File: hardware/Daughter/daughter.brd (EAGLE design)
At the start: 58.4 x 58.4 mm, 4 parts, among them J1 12V input

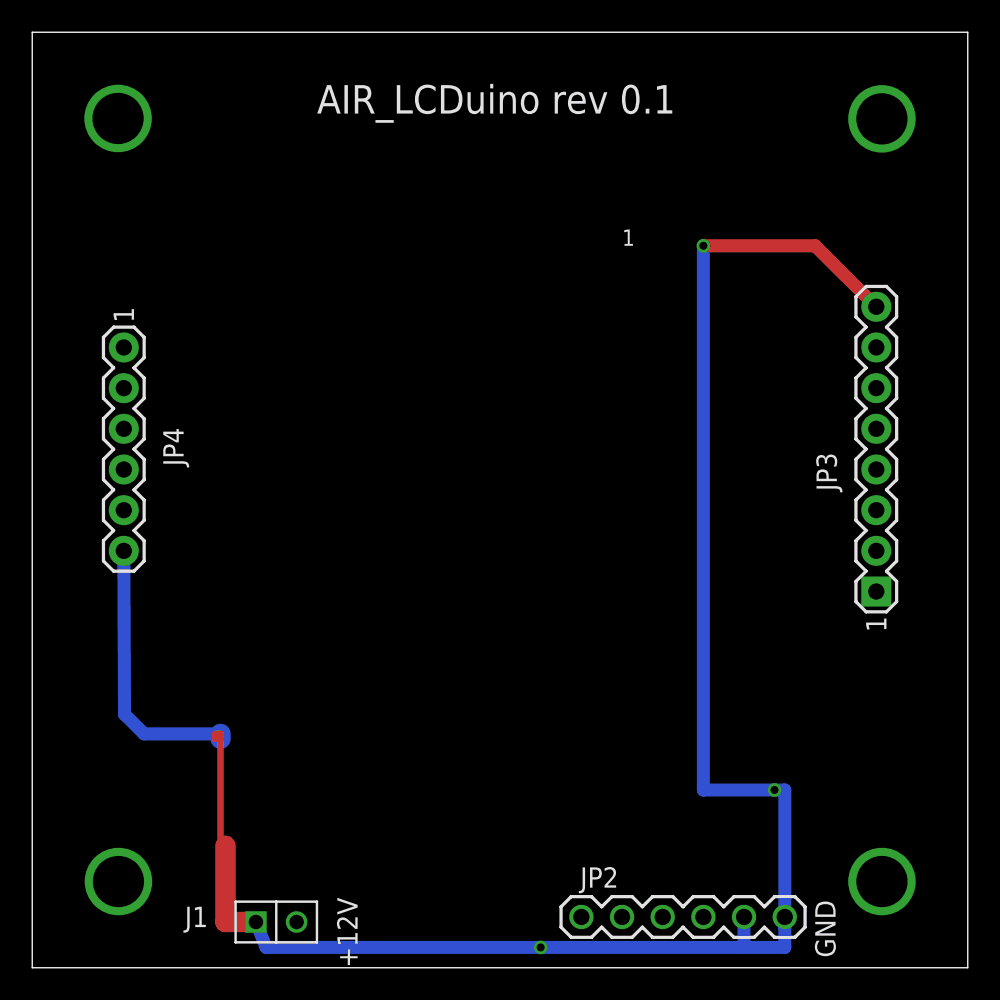
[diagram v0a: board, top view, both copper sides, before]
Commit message: added 12_adc_daughter/LTC2495_16x_pga_adc.pdf removed eagle.epf files and added gitignore file
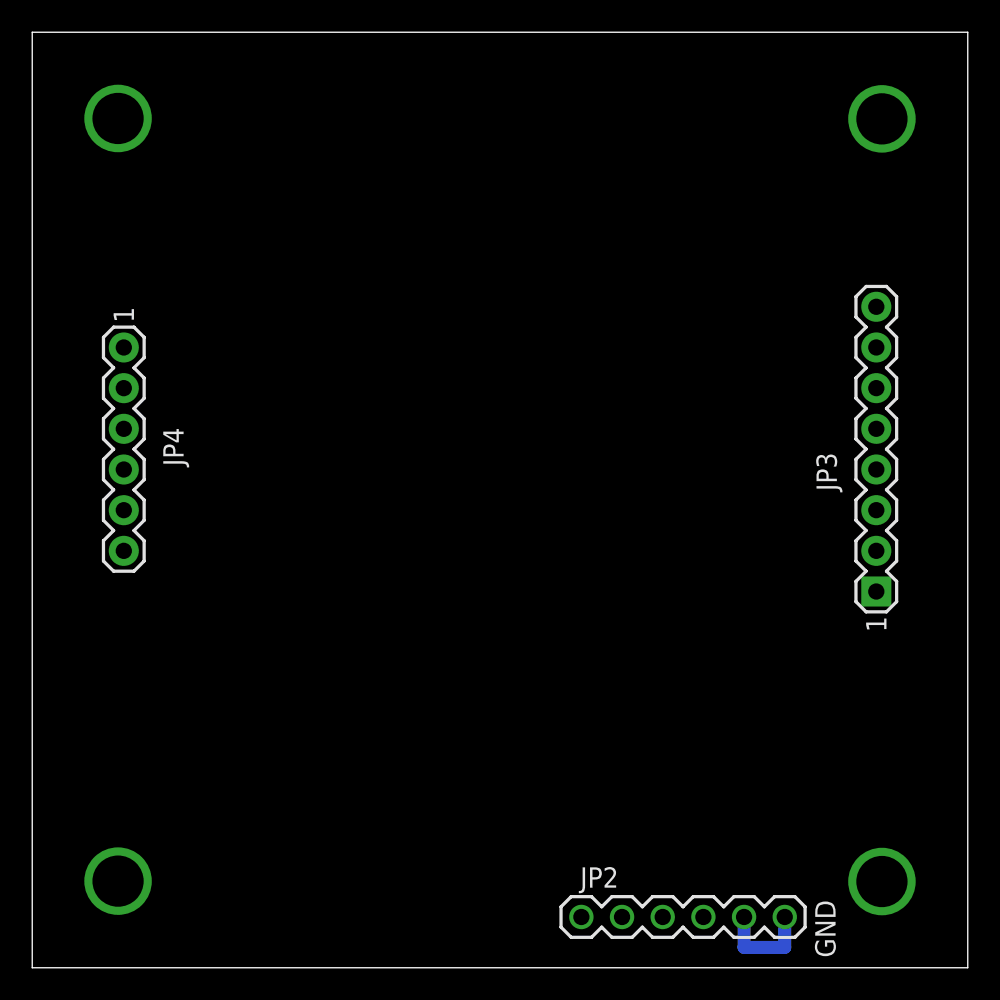
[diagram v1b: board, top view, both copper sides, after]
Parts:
- removed J1: 12V input, dp_devices:M1X2
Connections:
- removed net +12V: J1.2
- removed net +3.3V: JP4.5
- removed net +5V: JP3.1, JP4.1
- removed net RESET: JP3.2
- net GND: no longer J1.1, JP3.8, JP4.6
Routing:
- net GND: track 130.5 -> 6.34 mm, vias 3 -> 0
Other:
- board text removed: "+12V"
- board text removed: "1"
- board text removed: "AIR_LCDuino rev 0.1"
- board text removed: "RV-Builders Products"
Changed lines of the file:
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@@
 <board>
 <plain>
-<circle x="31.75" y="31.75" radius="28.448" width="0.0254" layer="199"/>
 <circle x="7.9248" y="55.5752" radius="1.524" width="0.0254" layer="199"/>
 <circle x="55.5752" y="55.5752" radius="1.524" width="0.0254" layer="199"/>
 <circle x="7.9248" y="7.9248" radius="1.524" width="0.0254" layer="199"/>
 <circle x="55.5752" y="7.9248" radius="1.524" width="0.0254" layer="199"/>
-<circle x="31.8516" y="16.51" radius="4.4958" width="0.0254" layer="199"/>
-<circle x="31.8516" y="16.51" radius="7.493" width="0.0254" layer="199"/>
-<circle x="15.875" y="16.8402" radius="2.5146" width="0.0254" layer="199"/>
-<circle x="13.7414" y="51.6128" radius="0.9906" width="0.0254" layer="199"/>
-<circle x="49.7586" y="51.6128" radius="0.9906" width="0.0254" layer="199"/>
-<circle x="13.7414" y="21.1074" radius="0.9144" width="0.0254" layer="199"/>
-<circle x="49.7586" y="21.1074" radius="0.9144" width="0.0254" layer="199"/>
-<wire x1="11.7602" y1="21.1074" x2="15.748" y2="21.1074" width="0.0254" layer="199" curve="180"/>
-<wire x1="47.752" y1="21.1074" x2="51.7398" y2="21.1074" width="0.0254" layer="199" curve="180"/>
-<wire x1="11.7602" y1="54.61" x2="51.7398" y2="54.61" width="0.0254" layer="199"/>
-<wire x1="11.7602" y1="21.082" x2="11.7602" y2="54.61" width="0.0254" layer="199"/>
-<wire x1="15.748" y1="21.1074" x2="15.748" y2="24.8666" width="0.0254" layer="199"/>
-<wire x1="47.752" y1="21.1074" x2="47.752" y2="24.8666" width="0.0254" layer="199"/>
-<wire x1="51.7398" y1="54.61" x2="51.7398" y2="21.1074" width="0.0254" layer="199"/>
-<circle x="31.8516" y="52.578" radius="0.2032" width="0.0254" layer="199"/>
-<circle x="31.8516" y="50.038" radius="0.2032" width="0.0254" layer="199"/>
-<circle x="34.3916" y="52.578" radius="0.2032" width="0.0254" layer="199"/>
-<circle x="34.3916" y="50.038" radius="0.2032" width="0.0254" layer="199"/>
-<circle x="36.9316" y="52.578" radius="0.2032" width="0.0254" layer="199"/>
-<circle x="36.9316" y="50.038" radius="0.2032" width="0.0254" layer="199"/>
-<circle x="39.4716" y="52.578" radius="0.2032" width="0.0254" layer="199"/>
-<circle x="39.4716" y="50.038" radius="0.2032" width="0.0254" layer="199"/>
-<circle x="29.3116" y="52.578" radius="0.2032" width="0.0254" layer="199"/>
-<circle x="29.3116" y="50.038" radius="0.2032" width="0.0254" layer="199"/>
-<circle x="26.7716" y="52.578" radius="0.2032" width="0.0254" layer="199"/>
-<circle x="26.7716" y="50.038" radius="0.2032" width="0.0254" layer="199"/>
-<circle x="24.2316" y="52.578" radius="0.2032" width="0.0254" layer="199"/>
-<circle x="24.2316" y="50.038" radius="0.2032" width="0.0254" layer="199"/>
-<circle x="47.625" y="16.8402" radius="2.5146" width="0.0254" layer="199"/>
-<wire x1="50.6476" y1="47.8536" x2="50.6476" y2="24.8666" width="0.0254" layer="199"/>
-<wire x1="50.6476" y1="24.8666" x2="12.8524" y2="24.8666" width="0.0254" layer="199"/>
-<wire x1="12.8524" y1="24.8666" x2="12.8524" y2="47.8536" width="0.0254" layer="199"/>
-<wire x1="45.3898" y1="54.6608" x2="45.3898" y2="47.8536" width="0.0254" layer="199"/>
-<wire x1="18.1102" y1="47.8536" x2="18.1102" y2="54.737" width="0.0254" layer="199"/>
-<wire x1="12.8524" y1="47.8536" x2="18.1102" y2="47.8536" width="0.0254" layer="199"/>
-<wire x1="45.3898" y1="47.8536" x2="50.6476" y2="47.8536" width="0.0254" layer="199"/>
 <wire x1="2.54" y1="60.96" x2="60.96" y2="60.96" width="0.0254" layer="20"/>
 <wire x1="60.96" y1="60.96" x2="60.96" y2="2.54" width="0.0254" layer="20"/>
 <wire x1="60.96" y1="2.54" x2="2.54" y2="2.54" width="0.0254" layer="20"/>
 <wire x1="2.54" y1="2.54" x2="2.54" y2="60.96" width="0.0254" layer="20"/>
-<wire x1="11.5062" y1="8.6106" x2="51.9938" y2="8.6106" width="0.0254" layer="199"/>
-<text x="22.86" y="2.54" size="1.27" layer="21" rot="R90">+12V </text>
 <text x="52.705" y="3.175" size="1.27" layer="21" rot="R90">GND</text>
-<text x="20.32" y="55.88" size="1.778" layer="21">AIR_LCDuino rev 0.1</text>
-<text x="43.18" y="56.515" size="1.778" layer="22" rot="MR0">RV-Builders Products</text>
-<text x="39.37" y="47.625" size="1.016" layer="21">1</text>
-<text x="39.37" y="47.625" size="1.016" layer="22" rot="MR0">1</text>
 </plain>
 <attributes>
@@
 </autorouter>
 <elements>
-<element name="J1" library="dp_devices" package="M1X2" value="12V input" x="17.78" y="5.3975" smashed="yes">
-<attribute name="NAME" x="12.065" y="5.08" size="1.27" layer="25" ratio="10"/>
-</element>
 <element name="JP2" library="SparkFun" package="1X06" value="5V UART" x="36.83130625" y="5.711515625" smashed="yes">
 <attribute name="NAME" x="36.75510625" y="7.540315625" size="1.27" layer="25" ratio="10"/>
@@
 <signal name="GND">
 <contactref element="JP2" pad="6"/>
-<contactref element="J1" pad="1"/>
-<contactref element="JP4" pad="6"/>
 <contactref element="JP2" pad="5"/>
-<contactref element="JP3" pad="8"/>
-<wire x1="44.45" y1="13.6398" x2="44.45" y2="47.625" width="0.8128" layer="16"/>
-<via x="44.45" y="47.625" extent="1-16" drill="0.5"/>
-<wire x1="51.435" y1="47.625" x2="44.45" y2="47.625" width="0.8128" layer="1"/>
-<wire x1="17.145" y1="3.81" x2="34.29" y2="3.81" width="0.8128" layer="16"/>
-<wire x1="55.248559375" y1="43.815165625" x2="51.435" y2="47.625" width="0.8128" layer="1"/>
-<wire x1="8.258740625" y1="28.5740875" x2="8.3058" y2="18.3642" width="0.8128" layer="16"/>
-<wire x1="8.3058" y1="18.3642" x2="9.525" y2="17.145" width="0.8128" layer="16"/>
-<wire x1="9.525" y1="17.145" x2="14.3002" y2="17.145" width="0.8128" layer="16"/>
 <wire x1="49.53130625" y1="3.81130625" x2="46.99" y2="3.81130625" width="0.8128" layer="16"/>
-<wire x1="49.53" y1="13.6398" x2="49.53" y2="5.08" width="0.8128" layer="16"/>
-<wire x1="49.53" y1="5.08" x2="49.53130625" y2="5.08" width="0.8128" layer="16"/>
-<wire x1="49.53130625" y1="5.08" x2="49.53130625" y2="5.711515625" width="0.8128" layer="16"/>
 <wire x1="49.53130625" y1="5.711515625" x2="49.53130625" y2="3.81130625" width="0.8128" layer="16"/>
 <wire x1="46.99130625" y1="5.711515625" x2="46.99" y2="5.711515625" width="0.8128" layer="16"/>
 <wire x1="46.99" y1="5.711515625" x2="46.99" y2="3.81130625" width="0.8128" layer="16"/>
-<wire x1="16.51" y1="5.3975" x2="17.145" y2="3.81" width="0.8128" layer="16"/>
-<via x="34.29" y="3.81" extent="1-16" drill="0.5"/>
-<wire x1="49.53" y1="13.6398" x2="48.895" y2="13.6398" width="0.8128" layer="16"/>
-<wire x1="48.895" y1="13.6398" x2="44.45" y2="13.6398" width="0.8128" layer="16"/>
-<via x="48.895" y="13.6398" extent="1-16" drill="0.5"/>
-<wire x1="14.605" y1="10.16" x2="14.605" y2="5.3975" width="1.27" layer="1"/>
-<wire x1="14.605" y1="5.3975" x2="16.51" y2="5.3975" width="1.27" layer="1"/>
-<wire x1="14.3002" y1="17.145" x2="14.3002" y2="16.8402" width="1.27" layer="16"/>
-<wire x1="34.29" y1="3.81" x2="46.99" y2="3.81" width="0.8128" layer="16"/>
-<wire x1="14.605" y1="10.16" x2="14.3002" y2="10.16" width="0.4064" layer="1"/>
-<wire x1="14.3002" y1="10.16" x2="14.3002" y2="16.8402" width="0.4064" layer="1"/>
-<wire x1="14.3002" y1="16.8402" x2="13.97" y2="16.8402" width="0.4064" layer="1"/>
-<wire x1="13.97" y1="16.8402" x2="13.97" y2="17.145" width="0.4064" layer="1"/>
-<wire x1="13.97" y1="17.145" x2="14.3002" y2="17.145" width="0.4064" layer="1"/>
-<wire x1="14.3002" y1="17.145" x2="14.3002" y2="16.8402" width="0.4064" layer="1"/>
-<wire x1="46.99" y1="3.81" x2="46.99" y2="3.81130625" width="0" layer="19" extent="16-16"/>
-<wire x1="14.3002" y1="17.145" x2="14.3002" y2="17.145" width="0" layer="19" extent="1-16"/>
 </signal>
 <signal name="N$3">
@@
 <signal name="N$4">
 <via x="7.8994" y="55.5752" extent="1-16" drill="3.2"/>
+<via x="7.8994" y="7.9502" extent="1-16" drill="3.2"/>
 </signal>
 <signal name="N$7">
 <via x="55.6006" y="7.9248" extent="1-16" drill="3.2"/>
 </signal>
-<signal name="N$8">
-<via x="7.9248" y="7.9248" extent="1-16" drill="3.2"/>
-</signal>
-<signal name="+5V">
-<contactref element="JP3" pad="1"/>
-<contactref element="JP4" pad="1"/>
-<wire x1="8.258740625" y1="41.2740875" x2="55.248559375" y2="26.035165625" width="0" layer="19" extent="1-1"/>
-</signal>
-<signal name="+3.3V">
-<contactref element="JP4" pad="5"/>
-</signal>
-<signal name="+12V">
-<contactref element="J1" pad="2"/>
-</signal>
-<signal name="RESET">
-<contactref element="JP3" pad="2"/>
-</signal>
 </signals>
